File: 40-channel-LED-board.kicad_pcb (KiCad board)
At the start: 2 copper layers, 50.2 x 23.5 mm, 44 parts, among them J1 CONN_40, P1 CONN_01X01

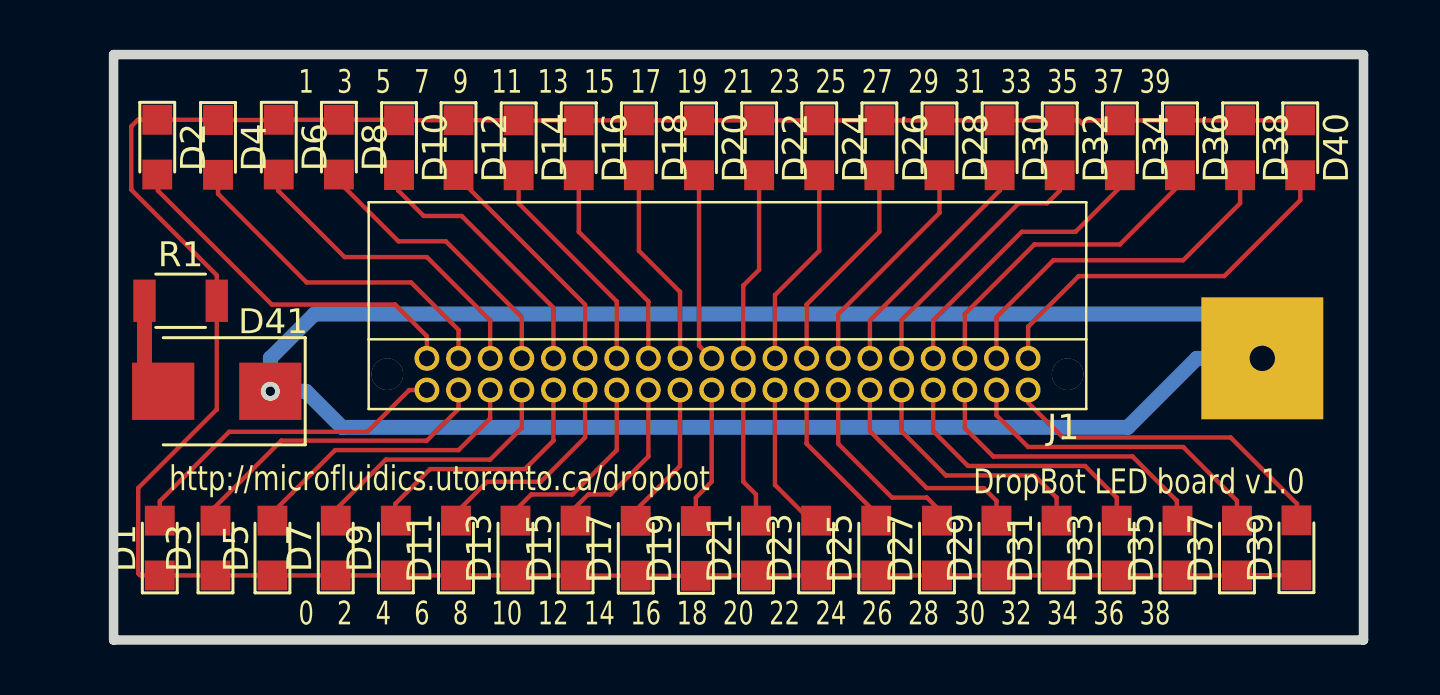
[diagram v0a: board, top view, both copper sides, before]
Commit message: Change trace width
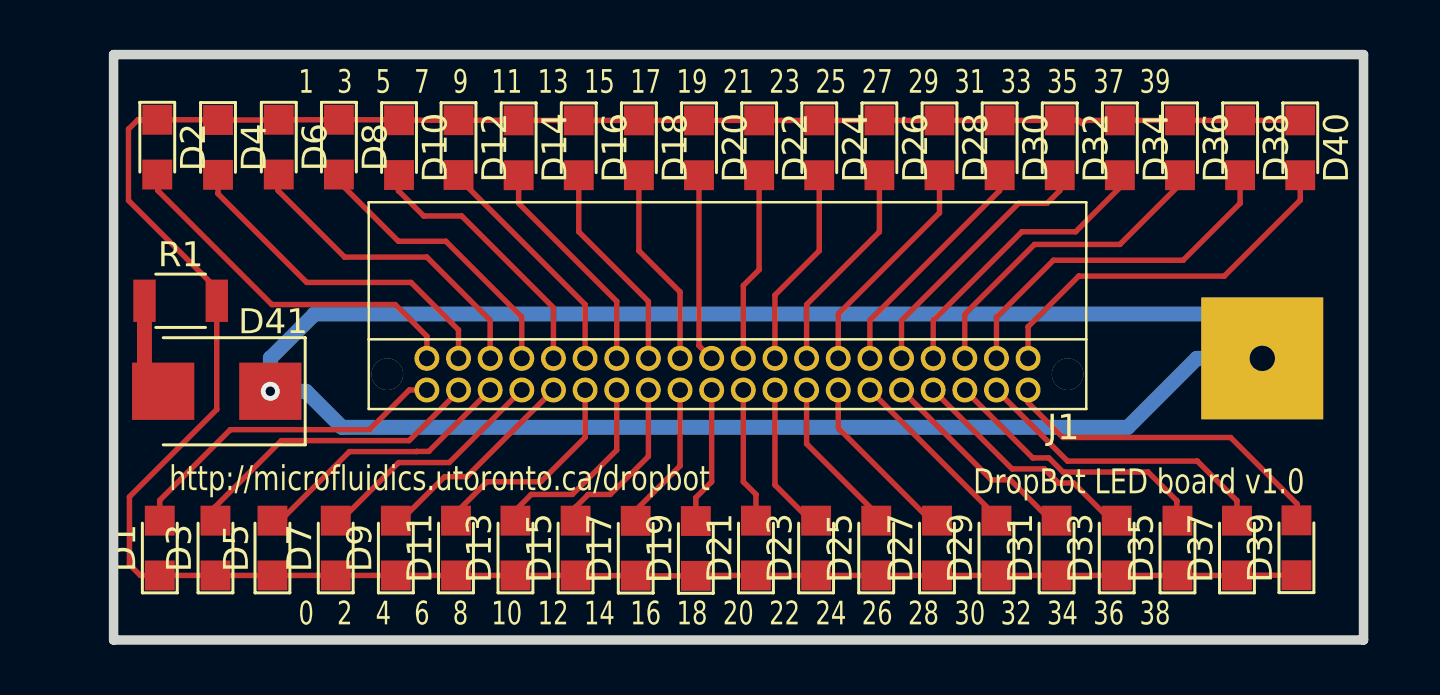
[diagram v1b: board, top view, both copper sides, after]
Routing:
- net Net-(D9-Pad2): track 10.3 -> 8.61 mm
- net Net-(D31-Pad2): track 10.1 -> 8.49 mm
- net Net-(D33-Pad2): track 11.3 -> 9.63 mm
- net Net-(D29-Pad2): track 8.90 -> 7.57 mm
- net Net-(D7-Pad2): track 11.0 -> 9.76 mm
- net Net-(D5-Pad2): track 11.9 -> 10.9 mm
- net Net-(D35-Pad2): track 12.3 -> 11.4 mm
- net Net-(D27-Pad2): track 7.91 -> 7.09 mm
- net Net-(D37-Pad2): track 13.1 -> 12.5 mm
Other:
- net class Default: clearance 0.1778 -> 0.22; trace_width 0.1778 -> 0.22
- rule trace_clearance: 0.1778 -> 0.22
- rule trace_min: 0.1778 -> 0.22
